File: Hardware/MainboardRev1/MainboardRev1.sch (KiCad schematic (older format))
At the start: 106 parts, among them J1 BACKUP_BATT: 1586038-2, J13 EXTRA_5V, J14 EXTRA_3V3, J2 MAIN_BATT: 1586038-2, Q1 SSM3J328R, Q10 SSM3J328R, Q11 NTR4003, Q12 NTR4003, Q13 NTR4003, Q2 SSM3J328R, Q3 SSM3J328R, Q4 SSM3J328R, Q5 NTR4003, Q6 NTR4003, Q7 NTR4003, Q8 SSM3J328R, Q9 NTR4003, SW1 EG2201A [DPDT], U1 LT6703-3, U2 LTC3605, U3 LTC4358, U4 LTC4358, U5 LDL1117S50R, U6 LDL1117S33R, U7 LTC2992, U8 LDL1117S33R, U9 LTC2992

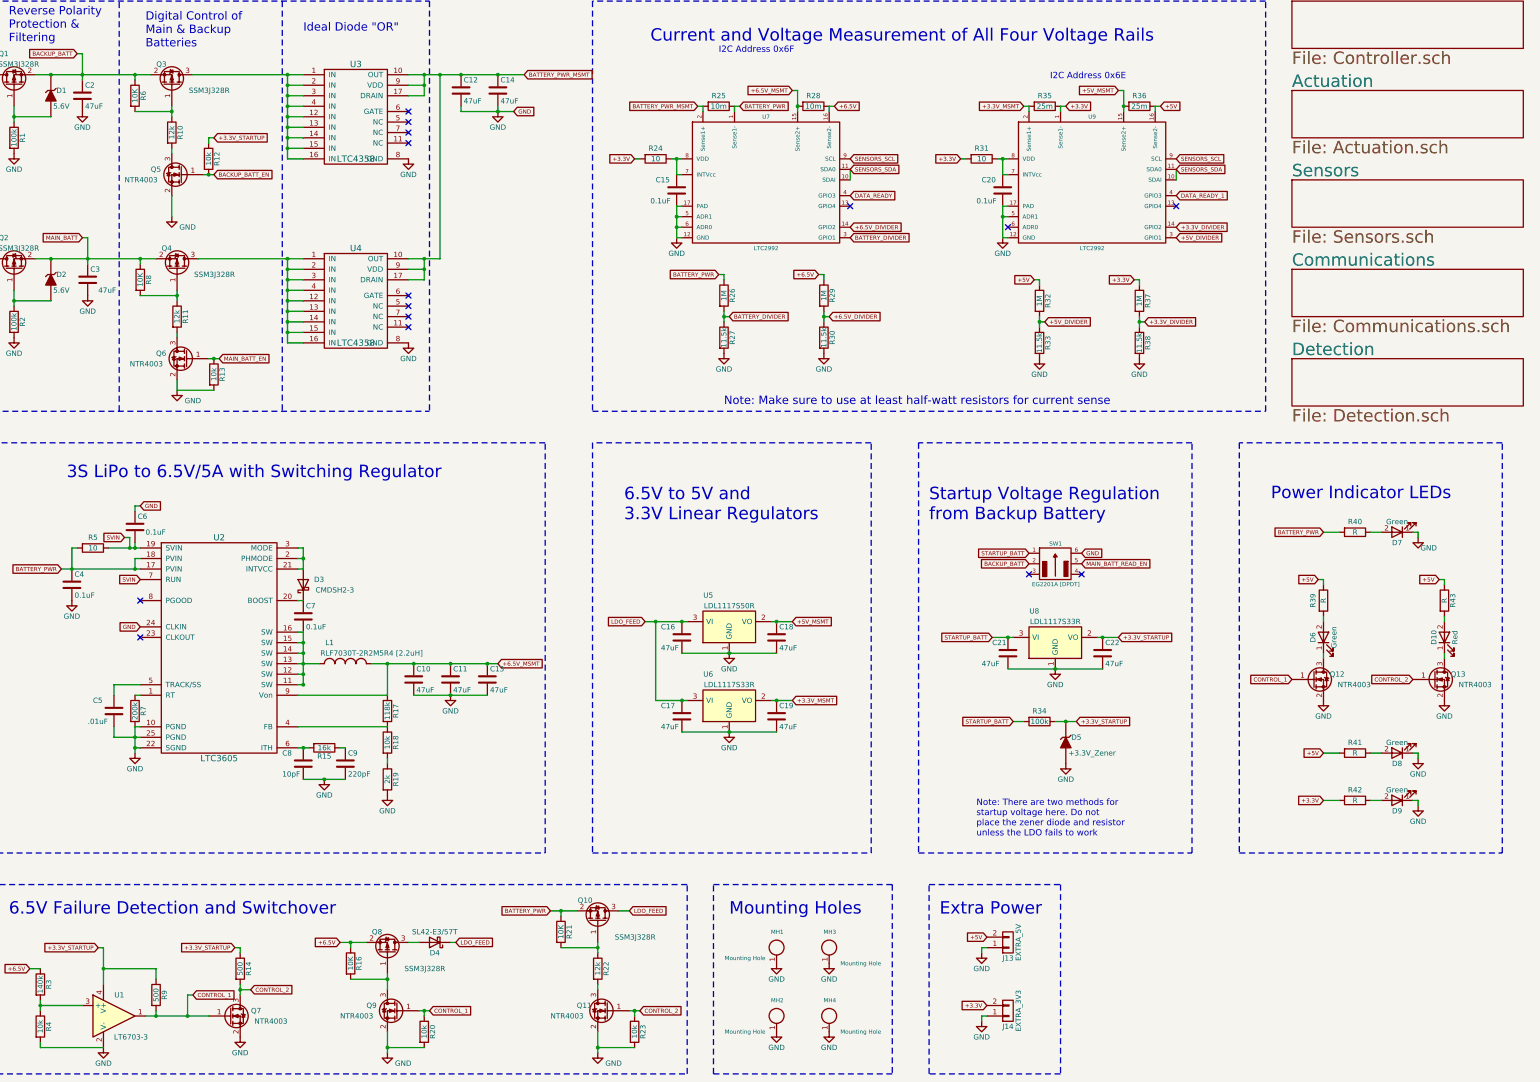
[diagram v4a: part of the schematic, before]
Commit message: Added buzzer and strobe LED. Created BOM. Reannotated. Added sponsors to silkscreen. Needs to be routed and sent out. Good luck Matt!
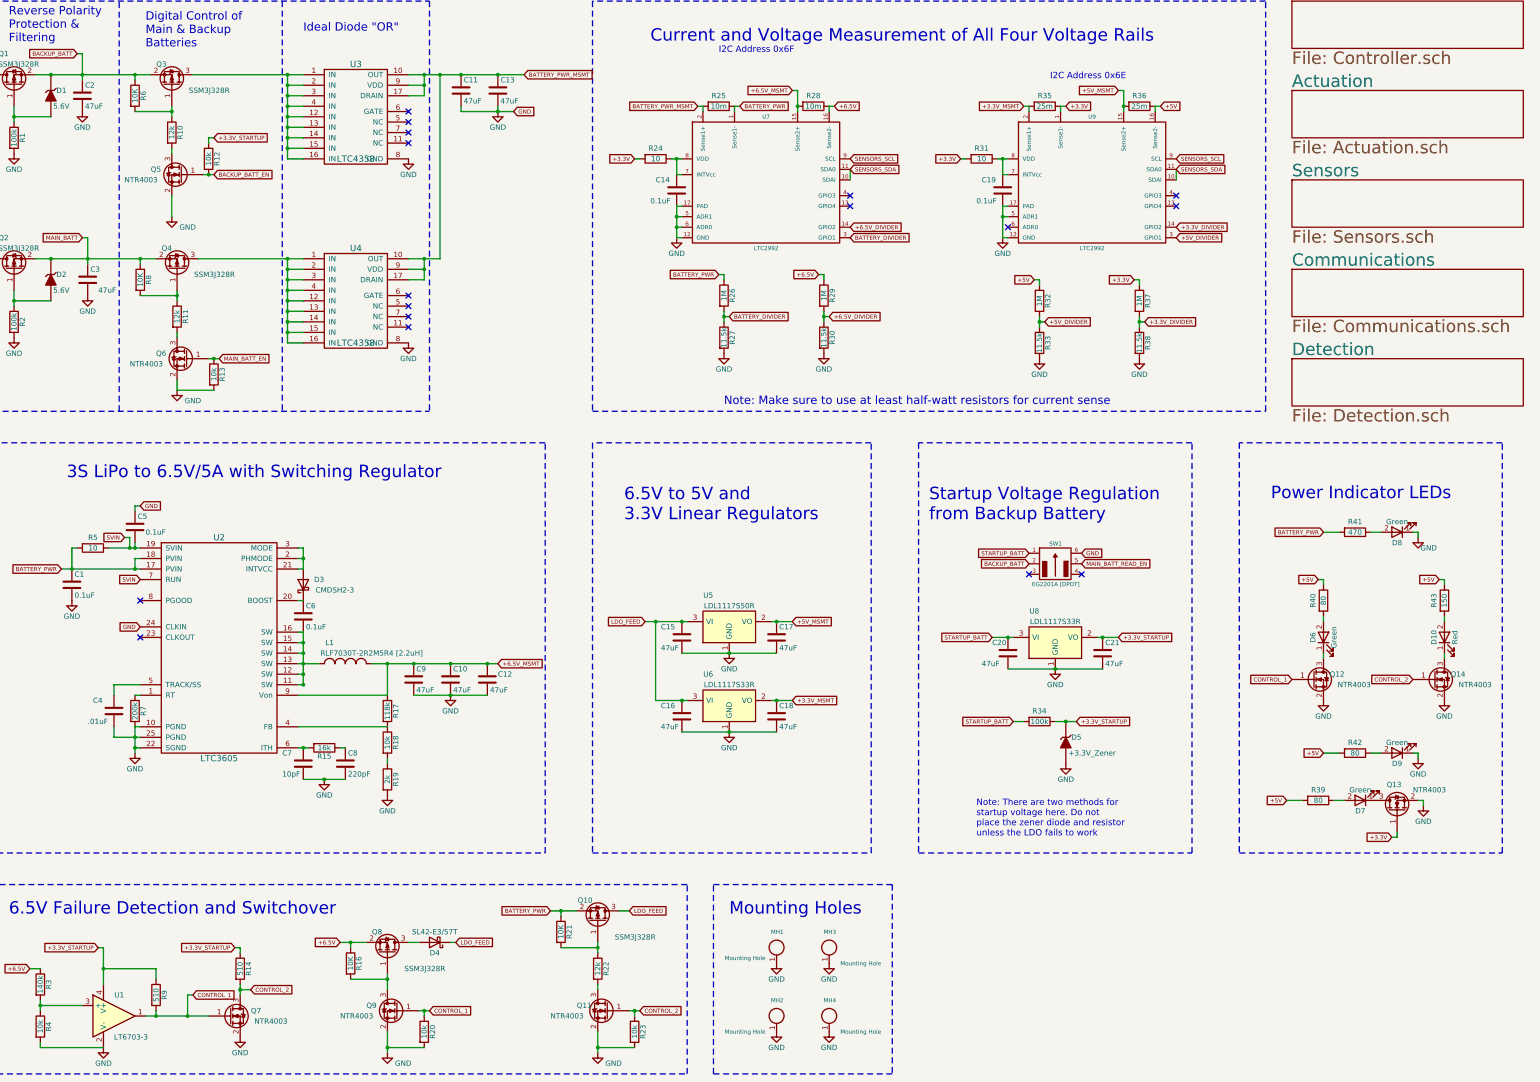
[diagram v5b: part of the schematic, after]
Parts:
- removed J13: EXTRA_5V, Dans_Parts:CONN_2POS_VERT_TE_CONN_LOCK_5-103669-1, symbol CONN_01X02
- removed J14: EXTRA_3V3, Dans_Parts:CONN_2POS_VERT_TE_CONN_LOCK_5-103669-1, symbol CONN_01X02
- added Q13: NTR4003, TO_SOT_Packages_SMD:SOT-23, symbol Q_NMOS_GSD
- R14, R9: value 500 -> 510
- R39: renamed from R42; value R -> 80
- R40: renamed from R39; value R -> 80
- R41: renamed from R40; value R -> 470
- R42: renamed from R41; value R -> 80
- R43: value R -> 150
- renumbered C4 to C1, C11 to C10, C12 to C11, C13 to C12, C14 to C13, C15 to C14, C16 to C15, C17 to C16, C18 to C17, C19 to C18, C20 to C19, C21 to C20, C22 to C21, C5 to C4, C6 to C5, C7 to C6, C8 to C7, C9 to C8, C10 to C9, D9 to D7, D7 to D8, D8 to D9, Q13 to Q14
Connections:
- net +3.3V: now also Q13.1 (G); no longer R39.2
- net +5V: now also R39.2
- net GND: now also Q13.2 (S); no longer D7.1 (K)
- net DATA_READY: no longer names the net of U7.4 (GPIO3)
- net DATA_READY_1: no longer names the net of U9.4 (GPIO3)
- new net: D7.1 (K), Q13.3 (D)
- no-connect marks 15 -> 17
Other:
- note removed: "Extra Power"
- moved on the sheet: D7, R39
